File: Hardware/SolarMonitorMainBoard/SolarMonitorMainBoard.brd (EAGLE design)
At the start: 100 x 78.7 mm, 50 parts, among them J2 ToTopPrint, J3 ISP, K1 RT314F12, K2 RT314F12, K3 RT314F12, U1 INA219AIDR, U10 TSR_1-2450, U2 INA219AIDR, U3 INA219AIDR, U4 INA219AIDR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

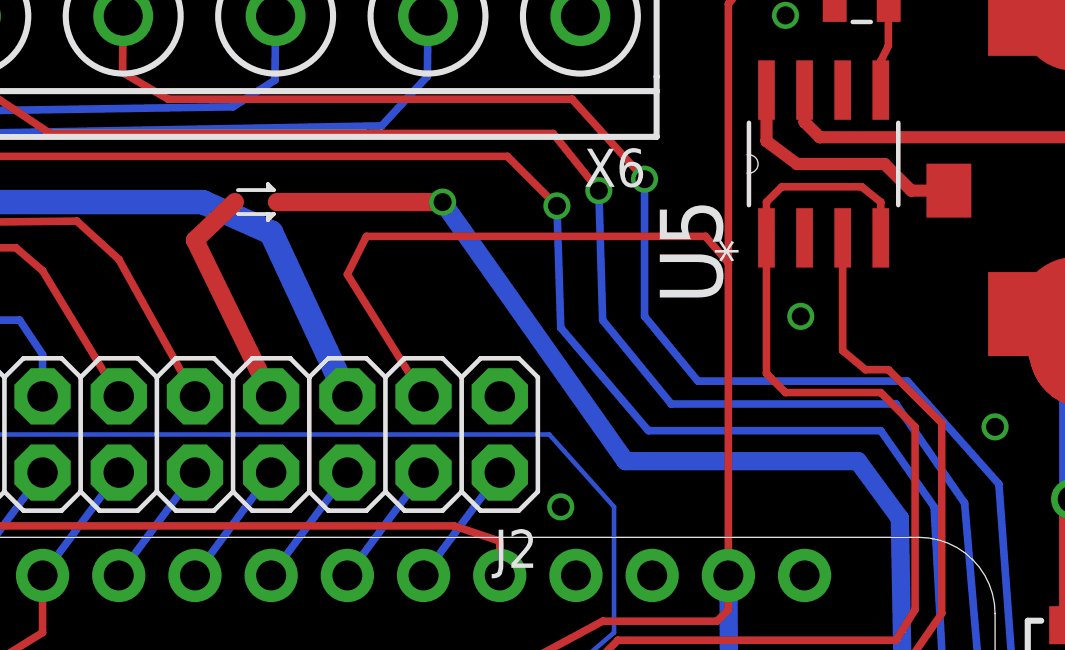
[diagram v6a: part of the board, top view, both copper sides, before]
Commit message: Replace BAT schottky with SMA part.
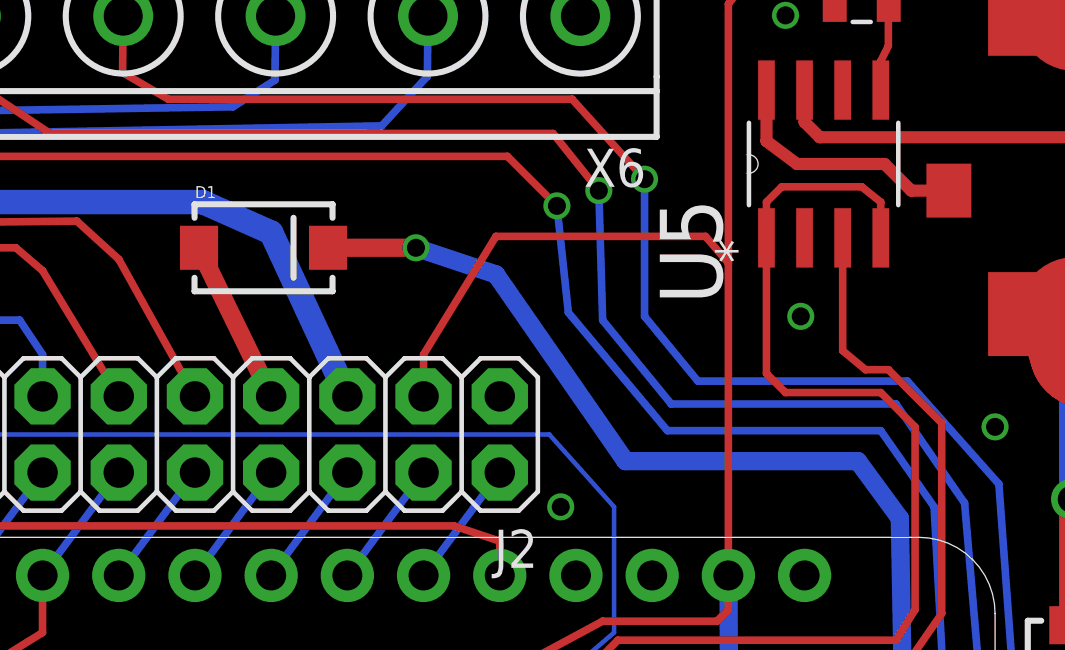
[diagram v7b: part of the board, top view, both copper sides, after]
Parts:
- D1: value RB751 -> B340A; device SparkFun-DiscreteSemi:SOD-523 -> SparkFun-DiscreteSemi:SMA-DIODE
- R11, R12, R13: value (none) -> 15k
- R21, R22, R23: value (none) -> 5.1k
- moved D1 1.55 mm to (27.7, 66.8)
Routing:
- net 3V: track 303.3 -> 298.7 mm
- net VBAT: track 61.3 -> 58.6 mm
- net FONA_BAT: track 7.63 -> 6.08 mm
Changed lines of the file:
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@@
 <element name="U10" library="_traco_tsr-1" package="TSR-1" value="TSR_1-2450" x="6.096" y="64.008" rot="R90"/>
 <element name="U$1" library="adafruit" package="MICROSD" value="MICROSD" x="85.09" y="17.399"/>
-<element name="D1" library="SparkFun-DiscreteSemi" package="SOD-523" value="RB751" x="27.432" y="68.326">
-<attribute name="PROD_ID" value="DIO-11018" x="27.432" y="68.326" size="1.778" layer="27" display="off"/>
+<element name="D1" library="SparkFun-DiscreteSemi" package="SMA-DIODE" value="B340A" x="27.686" y="66.802">
+<attribute name="PROD_ID" value="DIO-09886" x="27.686" y="66.802" size="1.778" layer="27" display="off"/>
 </element>
 <element name="R1" library="resistor-shunt" package="SMV" value="5m" x="13.97" y="18.542">
@@
 <element name="C7" library="SparkFun-Capacitors" package="0805" value="0.1uF" x="83.82" y="27.559"/>
 <element name="X6" library="con-phoenix-508" package="MKDSN1,5/8-5,08" value="MKDSN1,5/8-5,08" x="20.447" y="74.549" rot="R180"/>
-<element name="R11" library="SparkFun-Resistors" package="0805" value="" x="71.247" y="29.21" rot="R180"/>
-<element name="R21" library="SparkFun-Resistors" package="0805" value="" x="74.422" y="28.321" rot="R90"/>
+<element name="R11" library="SparkFun-Resistors" package="0805" value="15k" x="71.247" y="29.21" rot="R180"/>
+<element name="R21" library="SparkFun-Resistors" package="0805" value="5.1k" x="74.422" y="28.321" rot="R90"/>
 <element name="K1" library="relay" package="RT1-BI" value="RT314F12" x="93.218" y="63.119" rot="R90">
 <attribute name="MPN" value="RT314F12" x="93.218" y="63.119" size="1.778" layer="27" rot="R90" display="off"/>
@@
 <attribute name="OC_FARNELL" value="unknown" x="93.218" y="63.119" size="1.778" layer="27" rot="R90" display="off"/>
 </element>
-<element name="R12" library="SparkFun-Resistors" package="0805" value="" x="71.247" y="24.765" rot="R180"/>
-<element name="R22" library="SparkFun-Resistors" package="0805" value="" x="74.295" y="23.876" rot="R90"/>
-<element name="R13" library="SparkFun-Resistors" package="0805" value="" x="71.247" y="21.209" rot="R180"/>
-<element name="R23" library="SparkFun-Resistors" package="0805" value="" x="74.295" y="20.32" rot="R90"/>
+<element name="R12" library="SparkFun-Resistors" package="0805" value="15k" x="71.247" y="24.765" rot="R180"/>
+<element name="R22" library="SparkFun-Resistors" package="0805" value="5.1k" x="74.295" y="23.876" rot="R90"/>
+<element name="R13" library="SparkFun-Resistors" package="0805" value="15k" x="71.247" y="21.209" rot="R180"/>
+<element name="R23" library="SparkFun-Resistors" package="0805" value="5.1k" x="74.295" y="20.32" rot="R90"/>
 <element name="X5" library="con-phoenix-mkds_5" package="MKDS_5/3-762" value="MKDS_5/3-7,62" x="74.422" y="70.739" rot="R180">
 <attribute name="MPN" value="" x="74.422" y="70.739" size="1.778" layer="27" rot="R180" display="off"/>
@@
 <wire x1="48.133" y1="76.327" x2="48.514" y2="75.946" width="0.254" layer="1"/>
 <wire x1="48.514" y1="75.946" x2="48.514" y2="74.93" width="0.254" layer="1"/>
-<wire x1="33.02" y1="61.849" x2="30.48" y2="65.913" width="0.254" layer="1"/>
-<wire x1="30.48" y1="65.913" x2="31.115" y2="67.183" width="0.254" layer="1"/>
-<wire x1="31.115" y1="67.183" x2="42.418" y2="67.183" width="0.254" layer="1"/>
+<wire x1="33.02" y1="61.849" x2="33.02" y2="63.246" width="0.254" layer="1"/>
+<wire x1="33.02" y1="63.246" x2="35.433" y2="67.183" width="0.254" layer="1"/>
+<wire x1="35.433" y1="67.183" x2="42.418" y2="67.183" width="0.254" layer="1"/>
 <wire x1="42.418" y1="67.183" x2="43.18" y2="66.294" width="0.254" layer="1"/>
 </signal>
@@
 <wire x1="48.895" y1="57.785" x2="47.498" y2="59.69" width="0.6096" layer="16"/>
 <wire x1="47.498" y1="59.69" x2="39.751" y2="59.69" width="0.6096" layer="16"/>
-<wire x1="39.751" y1="59.69" x2="33.655" y2="68.326" width="0.6096" layer="16"/>
-<via x="33.655" y="68.326" extent="1-16" drill="0.6" shape="octagon"/>
-<wire x1="33.655" y1="68.326" x2="28.132" y2="68.326" width="0.6096" layer="1"/>
+<wire x1="39.751" y1="59.69" x2="35.433" y2="65.913" width="0.6096" layer="16"/>
+<wire x1="35.433" y1="65.913" x2="32.766" y2="66.802" width="0.6096" layer="16"/>
+<via x="32.766" y="66.802" extent="1-16" drill="0.6" shape="octagon"/>
+<wire x1="32.766" y1="66.802" x2="29.836" y2="66.802" width="0.6096" layer="1"/>
 </signal>
 <signal name="FONA_BAT">
@@
 <contactref element="J2" pad="7"/>
 <wire x1="27.94" y1="61.849" x2="25.4" y2="67.056" width="0.6096" layer="1"/>
-<wire x1="25.4" y1="67.056" x2="26.732" y2="68.326" width="0.6096" layer="1"/>
+<wire x1="25.4" y1="67.056" x2="25.536" y2="66.802" width="0.6096" layer="1"/>
 </signal>
 <signal name="N$11">
@@
 <wire x1="51.181" y1="36.83" x2="50.038" y2="58.166" width="0.254" layer="16"/>
 <wire x1="50.038" y1="58.166" x2="48.26" y2="60.706" width="0.254" layer="16"/>
-<wire x1="48.26" y1="60.706" x2="40.513" y2="60.706" width="0.254" layer="16"/>
-<wire x1="40.513" y1="60.706" x2="37.592" y2="64.135" width="0.254" layer="16"/>
-<wire x1="37.592" y1="64.135" x2="37.465" y2="68.199" width="0.254" layer="16"/>
+<wire x1="48.26" y1="60.706" x2="41.148" y2="60.706" width="0.254" layer="16"/>
+<wire x1="41.148" y1="60.706" x2="37.846" y2="64.643" width="0.254" layer="16"/>
+<wire x1="37.846" y1="64.643" x2="37.465" y2="68.199" width="0.254" layer="16"/>
 <via x="37.465" y="68.199" extent="1-16" drill="0.6" shape="octagon"/>
 <wire x1="37.465" y1="68.199" x2="35.814" y2="69.85" width="0.254" layer="1"/>

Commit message: Add some labels.
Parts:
- added U$2: (no value), SparkFun-Aesthetics:OSHW-LOGO-L
- moved D1 2.05 mm to (29.6, 66.0)
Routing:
- net VBAT: track 58.6 -> 56.5 mm
- net FONA_BAT: track 6.08 -> 4.25 mm
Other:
- board text added: "B1in"
- board text added: "B1out"
- board text added: "B2in"
- board text added: "BT SolarMonitor"
- board text added: "GND"
- board text added: "IO1"
- board text added: "IO2"
- board text added: "ISP"
- board text added: "L1"
- board text added: "L1in"
- board text added: "L2"
- board text added: "L2in"
- board text added: "Lon"
- board text added: "Lout"
- board text added: "P1in"
- board text added: "P1out"
- board text added: "P2in"
- board text added: "P2out"
- board text added: "RX"
- board text added: "T1"
- board text added: "T2"
- board text added: "Tx"
- board text added: "rev A"
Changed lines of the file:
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@@
 <layer number="25" name="tNames" color="7" fill="1" visible="yes" active="yes"/>
 <layer number="26" name="bNames" color="7" fill="1" visible="yes" active="yes"/>
-<layer number="27" name="tValues" color="7" fill="1" visible="yes" active="yes"/>
-<layer number="28" name="bValues" color="7" fill="1" visible="yes" active="yes"/>
+<layer number="27" name="tValues" color="7" fill="1" visible="no" active="yes"/>
+<layer number="28" name="bValues" color="7" fill="1" visible="no" active="yes"/>
 <layer number="29" name="tStop" color="7" fill="3" visible="no" active="yes"/>
 <layer number="30" name="bStop" color="7" fill="6" visible="no" active="yes"/>
@@
 <layer number="46" name="Milling" color="3" fill="1" visible="no" active="yes"/>
 <layer number="47" name="Measures" color="7" fill="1" visible="no" active="yes"/>
-<layer number="48" name="Document" color="7" fill="1" visible="yes" active="yes"/>
-<layer number="49" name="Reference" color="7" fill="1" visible="yes" active="yes"/>
+<layer number="48" name="Document" color="7" fill="1" visible="no" active="yes"/>
+<layer number="49" name="Reference" color="7" fill="1" visible="no" active="yes"/>
 <layer number="50" name="dxf" color="7" fill="1" visible="no" active="no"/>
 <layer number="51" name="tDocu" color="7" fill="1" visible="yes" active="yes"/>
@@
 <wire x1="0" y1="78.73" x2="0" y2="0" width="0" layer="20"/>
 <hole x="5" y="16.55" drill="2.8"/>
+<text x="9.652" y="13.589" size="1.016" layer="21">P1in</text>
+<text x="17.145" y="13.589" size="1.016" layer="21">P1out</text>
+<text x="24.892" y="13.589" size="1.016" layer="21">P2in</text>
+<text x="32.385" y="13.589" size="1.016" layer="21">P2out</text>
+<text x="40.132" y="13.589" size="1.016" layer="21">B1in</text>
+<text x="47.879" y="13.716" size="1.016" layer="21">B1out</text>
+<text x="55.245" y="13.589" size="1.016" layer="21">B2in</text>
+<text x="63.5" y="13.589" size="1.016" layer="21">P2out</text>
+<text x="72.39" y="64.77" size="1.016" layer="21" rot="SR0">Lout</text>
+<text x="76.962" y="64.643" size="1.016" layer="21" rot="SR0">L2in</text>
+<text x="81.28" y="64.77" size="1.016" layer="21" rot="SR0">L1in</text>
+<text x="14.732" y="48.133" size="1.6764" layer="21" font="vector">BT SolarMonitor</text>
+<text x="90.17" y="2.54" size="1.016" layer="22" rot="MR0">rev A</text>
+<wire x1="71.755" y1="64.135" x2="84.455" y2="64.135" width="0.127" layer="21"/>
+<wire x1="84.455" y1="64.135" x2="84.455" y2="68.58" width="0.127" layer="21"/>
+<wire x1="84.455" y1="68.58" x2="71.628" y2="68.58" width="0.127" layer="21"/>
+<wire x1="71.628" y1="68.58" x2="71.628" y2="64.135" width="0.127" layer="21"/>
+<wire x1="71.628" y1="64.135" x2="76.073" y2="64.135" width="0.127" layer="21"/>
+<wire x1="76.073" y1="64.135" x2="76.073" y2="68.453" width="0.127" layer="21"/>
+<wire x1="76.073" y1="68.453" x2="80.391" y2="68.453" width="0.127" layer="21"/>
+<wire x1="80.391" y1="68.453" x2="80.391" y2="64.262" width="0.127" layer="21"/>
+<text x="37.084" y="69.215" size="1.016" layer="21" rot="SR0">GND</text>
+<text x="32.385" y="69.215" size="1.016" layer="21" rot="SR0">T1</text>
+<text x="27.305" y="69.215" size="1.016" layer="21" rot="SR0">T2</text>
+<text x="22.352" y="69.215" size="1.016" layer="21" rot="SR0">L1</text>
+<text x="17.526" y="69.215" size="1.016" layer="21" rot="SR0">L2</text>
+<text x="11.684" y="69.215" size="1.016" layer="21" rot="SR0">Lon</text>
+<text x="6.858" y="69.215" size="1.016" layer="21" rot="SR0">IO1</text>
+<text x="1.524" y="69.215" size="1.016" layer="21" rot="SR0">IO2</text>
+<text x="79.121" y="14.351" size="1.016" layer="21">ISP</text>
+<text x="78.74" y="2.413" size="1.016" layer="21">RX</text>
+<text x="81.407" y="2.413" size="1.016" layer="21">Tx</text>
+<text x="70.231" y="13.716" size="1.016" layer="21">GND</text>
 </plain>
 <attributes>
@@
 <element name="U10" library="_traco_tsr-1" package="TSR-1" value="TSR_1-2450" x="6.096" y="64.008" rot="R90"/>
 <element name="U$1" library="adafruit" package="MICROSD" value="MICROSD" x="85.09" y="17.399"/>
-<element name="D1" library="SparkFun-DiscreteSemi" package="SMA-DIODE" value="B340A" x="27.686" y="66.802">
-<attribute name="PROD_ID" value="DIO-09886" x="27.686" y="66.802" size="1.778" layer="27" display="off"/>
+<element name="D1" library="SparkFun-DiscreteSemi" package="SMA-DIODE" value="B340A" x="29.591" y="66.04">
+<attribute name="PROD_ID" value="DIO-09886" x="29.591" y="66.04" size="1.778" layer="27" display="off"/>
 </element>
 <element name="R1" library="resistor-shunt" package="SMV" value="5m" x="13.97" y="18.542">
@@
 </element>
 <element name="R6" library="SparkFun-Resistors" package="0805" value="10k" x="77.343" y="8.509" rot="R90"/>
+<element name="U$2" library="SparkFun-Aesthetics" package="OSHW-LOGO-L" value="" x="95.25" y="3.81" rot="MR0"/>
 </elements>
 <signals>
@@
 <wire x1="47.498" y1="59.69" x2="39.751" y2="59.69" width="0.6096" layer="16"/>
 <wire x1="39.751" y1="59.69" x2="35.433" y2="65.913" width="0.6096" layer="16"/>
-<wire x1="35.433" y1="65.913" x2="32.766" y2="66.802" width="0.6096" layer="16"/>
-<via x="32.766" y="66.802" extent="1-16" drill="0.6" shape="octagon"/>
-<wire x1="32.766" y1="66.802" x2="29.836" y2="66.802" width="0.6096" layer="1"/>
+<wire x1="35.433" y1="65.913" x2="33.274" y2="66.04" width="0.6096" layer="16"/>
+<via x="33.274" y="66.04" extent="1-16" drill="0.6" shape="octagon"/>
+<wire x1="33.274" y1="66.04" x2="31.741" y2="66.04" width="0.6096" layer="1"/>
 </signal>
 <signal name="FONA_BAT">
 <contactref element="D1" pad="A"/>
 <contactref element="J2" pad="7"/>
-<wire x1="27.94" y1="61.849" x2="25.4" y2="67.056" width="0.6096" layer="1"/>
-<wire x1="25.4" y1="67.056" x2="25.536" y2="66.802" width="0.6096" layer="1"/>
+<wire x1="27.94" y1="61.849" x2="27.94" y2="63.881" width="0.6096" layer="1"/>
+<wire x1="27.94" y1="63.881" x2="27.441" y2="66.04" width="0.6096" layer="1"/>
 </signal>
 <signal name="N$11">
